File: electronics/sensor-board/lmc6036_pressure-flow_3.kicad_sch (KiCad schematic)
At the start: 12 parts, among them U14 LMC6036, U18 LMC6036

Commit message: work on sensor-board
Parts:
- removed U14, U18: LMC6036, LMC6036:SOP65P640X120-14N, symbol LMC6036_custom:LMC6036
- added U11: LMC6036, LMC6036:SOP65P640X120-14N, symbol LMC6036_custom:LMC6036
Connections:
- net VDD: now also U11.4 (VDD)
- net VSS: now also U11.11 (VSS)
- net output_A: now also U11.1 (OUTA), U11.2 (INA-)
- net output_B: now also U11.6 (INB-), U11.7 (OUTB)
- net output_C: now also U11.8 (OUTC), U11.9 (INC-)
- net output_D: now also U11.14 (OUTD)
- net at R103.1, R99.1: now also U11.5 (INB+)
- net at R101.1, R105.1: now also U11.12 (IND+)
- net at R106.1, R107.2: now also U11.13 (IND-)
- net at R100.1, R104.1: now also U11.10 (INC+)
- net at R102.1, R98.1: now also U11.3 (INA+)
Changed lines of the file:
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@@
   (junction (at 142.24 120.65) (diameter 0) (color 0 0 0 0))
   (junction (at 142.24 148.59) (diameter 0) (color 0 0 0 0))
-  (junction (at 147.32 143.51) (diameter 0) (color 0 0 0 0))
-  (junction (at 162.56 63.5) (diameter 0) (color 0 0 0 0))
-  (junction (at 162.56 90.17) (diameter 0) (color 0 0 0 0))
-  (junction (at 162.56 118.11) (diameter 0) (color 0 0 0 0))
-  (junction (at 162.56 146.05) (diameter 0) (color 0 0 0 0))
   (wire (pts (xy 125.73 60.96) (xy 135.89 60.96))
     (stroke (width 0) (type default) (color 0 0 0 0))
@@
   )
   (symbol (lib_id "Device:R") (at 135.89 148.59 270) (unit 1)
-    (in_bom yes) (on_board yes) (fields_autoplaced)
+    (in_bom yes) (on_board yes)
     (property "Reference" "R101" (id 0) (at 135.89 142.24 90))
-    (property "Value" "NO_RES" (id 1) (at 135.89 144.78 90))
+    (property "Value" "NO_RES" (id 1) (at 135.89 146.05 90))
     (property "Footprint" "Resistor_SMD:R_0603_1608Metric" (id 2) (at 135.89 146.812 90)
       (effects (font (size 1.27 1.27)) hide)
@@
   (symbol (lib_id "LMC6036_custom:LMC6036") (at 153.67 44.45 90) (unit 5)
     (in_bom yes) (on_board yes) (fields_autoplaced)
-    (property "Reference" "U14" (id 0) (at 153.67 35.56 90))
+    (property "Reference" "U11" (id 0) (at 153.67 35.56 90))
     (property "Value" "LMC6036" (id 1) (at 153.67 38.1 90))
     (property "Footprint" "LMC6036:SOP65P640X120-14N" (id 2) (at 153.67 42.545 0)
@@
   )
   (symbol (lib_id "LMC6036_custom:LMC6036") (at 153.67 63.5 0) (unit 1)
-    (in_bom yes) (on_board yes)
-    (property "Reference" "U18" (id 0) (at 154.94 53.34 0))
-    (property "Value" "LMC6036" (id 1) (at 160.02 68.58 0))
+    (in_bom yes) (on_board yes) (fields_autoplaced)
+    (property "Reference" "U11" (id 0) (at 154.94 53.34 0))
+    (property "Value" "LMC6036" (id 1) (at 154.94 55.88 0))
     (property "Footprint" "LMC6036:SOP65P640X120-14N" (id 2) (at 155.575 63.5 0)
       (effects (font (size 1.27 1.27)) hide)
@@
   (symbol (lib_id "LMC6036_custom:LMC6036") (at 153.67 90.17 0) (unit 2)
     (in_bom yes) (on_board yes) (fields_autoplaced)
-    (property "Reference" "U14" (id 0) (at 154.94 80.01 0))
+    (property "Reference" "U11" (id 0) (at 154.94 80.01 0))
     (property "Value" "LMC6036" (id 1) (at 154.94 82.55 0))
     (property "Footprint" "LMC6036:SOP65P640X120-14N" (id 2) (at 155.575 90.17 0)
@@
   (symbol (lib_id "LMC6036_custom:LMC6036") (at 153.67 118.11 0) (unit 3)
     (in_bom yes) (on_board yes) (fields_autoplaced)
-    (property "Reference" "U14" (id 0) (at 154.94 107.95 0))
+    (property "Reference" "U11" (id 0) (at 154.94 107.95 0))
     (property "Value" "LMC6036" (id 1) (at 154.94 110.49 0))
     (property "Footprint" "LMC6036:SOP65P640X120-14N" (id 2) (at 155.575 118.11 0)
@@
   (symbol (lib_id "LMC6036_custom:LMC6036") (at 153.67 146.05 0) (unit 4)
     (in_bom yes) (on_board yes)
-    (property "Reference" "U14" (id 0) (at 154.94 135.89 0))
-    (property "Value" "LMC6036" (id 1) (at 152.4 146.05 0))
+    (property "Reference" "U11" (id 0) (at 154.94 135.89 0))
+    (property "Value" "LMC6036" (id 1) (at 154.94 140.97 0))
     (property "Footprint" "LMC6036:SOP65P640X120-14N" (id 2) (at 155.575 146.05 0)
       (effects (font (size 1.27 1.27)) hide)

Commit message: work on sensor-board pcb
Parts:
- removed R101, R105, R106, R107: NO_RES, Resistor_SMD:R_0603_1608Metric, symbol Device:R
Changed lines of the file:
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@@
-    (pin "2")
-  )
-  (symbol (lib_id "Device:R") (at 135.89 143.51 270) (unit 1)
-    (in_bom yes) (on_board yes) (fields_autoplaced)
-    (property "Reference" "R106" (id 0) (at 135.89 137.16 90))
-    (property "Value" "NO_RES" (id 1) (at 135.89 139.7 90))
-    (property "Footprint" "Resistor_SMD:R_0603_1608Metric" (id 2) (at 135.89 141.732 90)
-      (effects (font (size 1.27 1.27)) hide)
-    )
-    (property "Datasheet" "~" (id 3) (at 135.89 143.51 0)
-      (effects (font (size 1.27 1.27)) hide)
-    )
-    (pin "1")
-    (pin "2")
-  )
-  (symbol (lib_id "Device:R") (at 135.89 148.59 270) (unit 1)
-    (in_bom yes) (on_board yes)
-    (property "Reference" "R101" (id 0) (at 135.89 142.24 90))
-    (property "Value" "NO_RES" (id 1) (at 135.89 146.05 90))
-    (property "Footprint" "Resistor_SMD:R_0603_1608Metric" (id 2) (at 135.89 146.812 90)
-      (effects (font (size 1.27 1.27)) hide)
-    )
-    (property "Datasheet" "~" (id 3) (at 135.89 148.59 0)
-      (effects (font (size 1.27 1.27)) hide)
-    )
-    (pin "1")
     (pin "2")
   )
@@
       (effects (font (size 1.27 1.27)) hide)
     )
-    (pin "1")
-    (pin "2")
-  )
-  (symbol (lib_id "Device:R") (at 142.24 153.67 0) (unit 1)
-    (in_bom yes) (on_board yes) (fields_autoplaced)
-    (property "Reference" "R105" (id 0) (at 144.78 152.3999 0)
-      (effects (font (size 1.27 1.27)) (justify left))
-    )
-    (property "Value" "NO_RES" (id 1) (at 144.78 154.9399 0)
-      (effects (font (size 1.27 1.27)) (justify left))
-    )
-    (property "Footprint" "Resistor_SMD:R_0603_1608Metric" (id 2) (at 140.462 153.67 90)
-      (effects (font (size 1.27 1.27)) hide)
-    )
-    (property "Datasheet" "~" (id 3) (at 142.24 153.67 0)
-      (effects (font (size 1.27 1.27)) hide)
-    )
-    (pin "1")
-    (pin "2")
-  )
-  (symbol (lib_id "Device:R") (at 154.94 138.43 270) (unit 1)
-    (in_bom yes) (on_board yes) (fields_autoplaced)
-    (property "Reference" "R107" (id 0) (at 154.94 132.08 90))
-    (property "Value" "NO_RES" (id 1) (at 154.94 134.62 90))
-    (property "Footprint" "Resistor_SMD:R_0603_1608Metric" (id 2) (at 154.94 136.652 90)
-      (effects (font (size 1.27 1.27)) hide)
-    )
-    (property "Datasheet" "~" (id 3) (at 154.94 138.43 0)
-      (effects (font (size 1.27 1.27)) hide)
-    )

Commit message: More work on sensor-board
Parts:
- R100, R103, R104, R98, R99: value 150 -> 100
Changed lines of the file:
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@@
       (effects (font (size 1.27 1.27)) (justify left))
     )
-    (property "Value" "150" (id 1) (at 144.78 99.0599 0)
+    (property "Value" "100" (id 1) (at 144.78 99.0599 0)
       (effects (font (size 1.27 1.27)) (justify left))
     )
@@
     (in_bom yes) (on_board yes) (fields_autoplaced)
     (property "Reference" "R99" (id 0) (at 135.89 86.36 90))
-    (property "Value" "150" (id 1) (at 135.89 88.9 90))
+    (property "Value" "100" (id 1) (at 135.89 88.9 90))
     (property "Footprint" "Resistor_SMD:R_0603_1608Metric" (id 2) (at 135.89 90.932 90)
       (effects (font (size 1.27 1.27)) hide)
@@
     (in_bom yes) (on_board yes) (fields_autoplaced)
     (property "Reference" "R100" (id 0) (at 135.89 114.3 90))
-    (property "Value" "150" (id 1) (at 135.89 116.84 90))
+    (property "Value" "100" (id 1) (at 135.89 116.84 90))
     (property "Footprint" "Resistor_SMD:R_0603_1608Metric" (id 2) (at 135.89 118.872 90)
       (effects (font (size 1.27 1.27)) hide)
@@
     (in_bom yes) (on_board yes) (fields_autoplaced)
     (property "Reference" "R98" (id 0) (at 135.89 59.69 90))
-    (property "Value" "150" (id 1) (at 135.89 62.23 90))
+    (property "Value" "100" (id 1) (at 135.89 62.23 90))
     (property "Footprint" "Resistor_SMD:R_0603_1608Metric" (id 2) (at 135.89 64.262 90)
       (effects (font (size 1.27 1.27)) hide)
@@
       (effects (font (size 1.27 1.27)) (justify left))
     )
-    (property "Value" "150" (id 1) (at 144.78 126.9999 0)
+    (property "Value" "100" (id 1) (at 144.78 126.9999 0)
       (effects (font (size 1.27 1.27)) (justify left))
     )

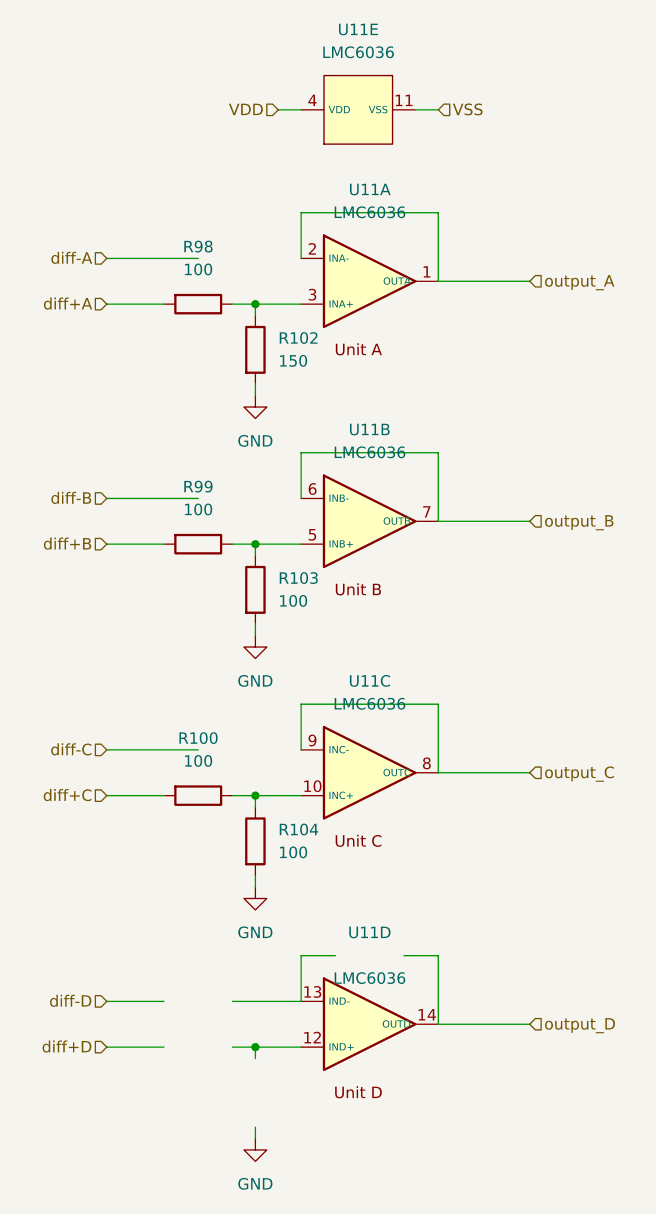
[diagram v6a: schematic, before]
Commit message: updated loadcell amplifier
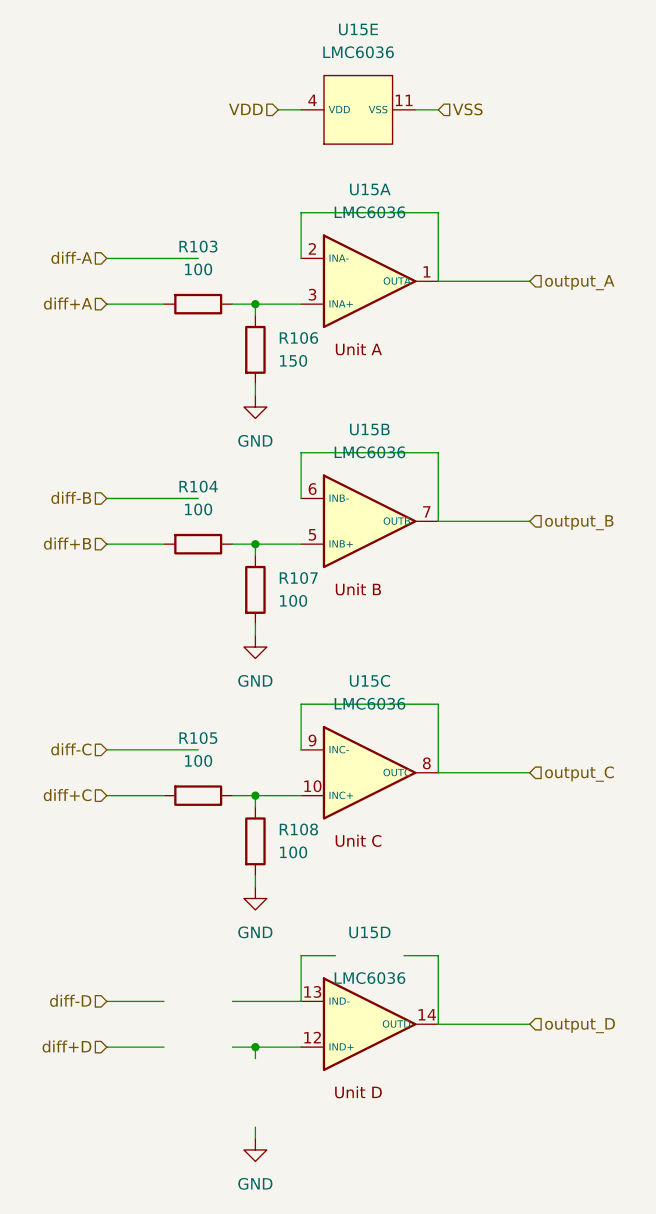
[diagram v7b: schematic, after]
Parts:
- renumbered R98 to R103, R99 to R104, R100 to R105, R102 to R106, R103 to R107, R104 to R108, U11 to U15
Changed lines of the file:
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@@
   (symbol (lib_id "power:GND") (at 142.24 158.75 0) (unit 1)
     (in_bom yes) (on_board yes) (fields_autoplaced)
-    (property "Reference" "#PWR0134" (id 0) (at 142.24 165.1 0)
+    (property "Reference" "#PWR0149" (id 0) (at 142.24 165.1 0)
       (effects (font (size 1.27 1.27)) hide)
     )
@@
   (symbol (lib_id "Device:R") (at 142.24 97.79 0) (unit 1)
     (in_bom yes) (on_board yes) (fields_autoplaced)
-    (property "Reference" "R103" (id 0) (at 144.78 96.5199 0)
+    (property "Reference" "R107" (id 0) (at 144.78 96.5199 0)
       (effects (font (size 1.27 1.27)) (justify left))
     )
@@
   (symbol (lib_id "power:GND") (at 142.24 76.2 0) (unit 1)
     (in_bom yes) (on_board yes) (fields_autoplaced)
-    (property "Reference" "#PWR0131" (id 0) (at 142.24 82.55 0)
+    (property "Reference" "#PWR0146" (id 0) (at 142.24 82.55 0)
       (effects (font (size 1.27 1.27)) hide)
     )
@@
   (symbol (lib_id "Device:R") (at 135.89 92.71 270) (unit 1)
     (in_bom yes) (on_board yes) (fields_autoplaced)
-    (property "Reference" "R99" (id 0) (at 135.89 86.36 90))
+    (property "Reference" "R104" (id 0) (at 135.89 86.36 90))
     (property "Value" "100" (id 1) (at 135.89 88.9 90))
     (property "Footprint" "Resistor_SMD:R_0603_1608Metric" (id 2) (at 135.89 90.932 90)
@@
   (symbol (lib_id "LMC6036_custom:LMC6036") (at 153.67 146.05 0) (unit 4)
     (in_bom yes) (on_board yes)
-    (property "Reference" "U11" (id 0) (at 154.94 135.89 0))
+    (property "Reference" "U15" (id 0) (at 154.94 135.89 0))
     (property "Value" "LMC6036" (id 1) (at 154.94 140.97 0))
     (property "Footprint" "LMC6036:SOP65P640X120-14N" (id 2) (at 155.575 146.05 0)
@@
   (symbol (lib_id "Device:R") (at 135.89 120.65 270) (unit 1)
     (in_bom yes) (on_board yes) (fields_autoplaced)
-    (property "Reference" "R100" (id 0) (at 135.89 114.3 90))
+    (property "Reference" "R105" (id 0) (at 135.89 114.3 90))
     (property "Value" "100" (id 1) (at 135.89 116.84 90))
     (property "Footprint" "Resistor_SMD:R_0603_1608Metric" (id 2) (at 135.89 118.872 90)
@@
   (symbol (lib_id "LMC6036_custom:LMC6036") (at 153.67 63.5 0) (unit 1)
     (in_bom yes) (on_board yes) (fields_autoplaced)
-    (property "Reference" "U11" (id 0) (at 154.94 53.34 0))
+    (property "Reference" "U15" (id 0) (at 154.94 53.34 0))
     (property "Value" "LMC6036" (id 1) (at 154.94 55.88 0))
     (property "Footprint" "LMC6036:SOP65P640X120-14N" (id 2) (at 155.575 63.5 0)
@@
   (symbol (lib_id "power:GND") (at 142.24 130.81 0) (unit 1)
     (in_bom yes) (on_board yes) (fields_autoplaced)
-    (property "Reference" "#PWR0133" (id 0) (at 142.24 137.16 0)
+    (property "Reference" "#PWR0148" (id 0) (at 142.24 137.16 0)
       (effects (font (size 1.27 1.27)) hide)
     )
@@
   (symbol (lib_id "Device:R") (at 135.89 66.04 270) (unit 1)
     (in_bom yes) (on_board yes) (fields_autoplaced)
-    (property "Reference" "R98" (id 0) (at 135.89 59.69 90))
+    (property "Reference" "R103" (id 0) (at 135.89 59.69 90))
     (property "Value" "100" (id 1) (at 135.89 62.23 90))
     (property "Footprint" "Resistor_SMD:R_0603_1608Metric" (id 2) (at 135.89 64.262 90)
@@
   (symbol (lib_id "power:GND") (at 142.24 102.87 0) (unit 1)
     (in_bom yes) (on_board yes) (fields_autoplaced)
-    (property "Reference" "#PWR0132" (id 0) (at 142.24 109.22 0)
+    (property "Reference" "#PWR0147" (id 0) (at 142.24 109.22 0)
       (effects (font (size 1.27 1.27)) hide)
     )
@@
   (symbol (lib_id "LMC6036_custom:LMC6036") (at 153.67 90.17 0) (unit 2)
     (in_bom yes) (on_board yes) (fields_autoplaced)
-    (property "Reference" "U11" (id 0) (at 154.94 80.01 0))
+    (property "Reference" "U15" (id 0) (at 154.94 80.01 0))
     (property "Value" "LMC6036" (id 1) (at 154.94 82.55 0))
     (property "Footprint" "LMC6036:SOP65P640X120-14N" (id 2) (at 155.575 90.17 0)
@@
   (symbol (lib_id "LMC6036_custom:LMC6036") (at 153.67 44.45 90) (unit 5)
     (in_bom yes) (on_board yes) (fields_autoplaced)
-    (property "Reference" "U11" (id 0) (at 153.67 35.56 90))
+    (property "Reference" "U15" (id 0) (at 153.67 35.56 90))
     (property "Value" "LMC6036" (id 1) (at 153.67 38.1 90))
     (property "Footprint" "LMC6036:SOP65P640X120-14N" (id 2) (at 153.67 42.545 0)
@@
   (symbol (lib_id "Device:R") (at 142.24 125.73 0) (unit 1)
     (in_bom yes) (on_board yes) (fields_autoplaced)
-    (property "Reference" "R104" (id 0) (at 144.78 124.4599 0)
+    (property "Reference" "R108" (id 0) (at 144.78 124.4599 0)
       (effects (font (size 1.27 1.27)) (justify left))
     )
@@
   (symbol (lib_id "LMC6036_custom:LMC6036") (at 153.67 118.11 0) (unit 3)
     (in_bom yes) (on_board yes) (fields_autoplaced)
-    (property "Reference" "U11" (id 0) (at 154.94 107.95 0))
+    (property "Reference" "U15" (id 0) (at 154.94 107.95 0))
     (property "Value" "LMC6036" (id 1) (at 154.94 110.49 0))
     (property "Footprint" "LMC6036:SOP65P640X120-14N" (id 2) (at 155.575 118.11 0)
@@
   (symbol (lib_id "Device:R") (at 142.24 71.12 0) (unit 1)
     (in_bom yes) (on_board yes) (fields_autoplaced)
-    (property "Reference" "R102" (id 0) (at 144.78 69.8499 0)
-      (effects (font (size 1.27 1.27)) (justify left))
-    )
+    (property "Reference" "R106" (id 0) (at 144.78 69.8499 0)
+      (effects (font (size 1.27 1.27)) (justify left))
+    )

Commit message: res value fix
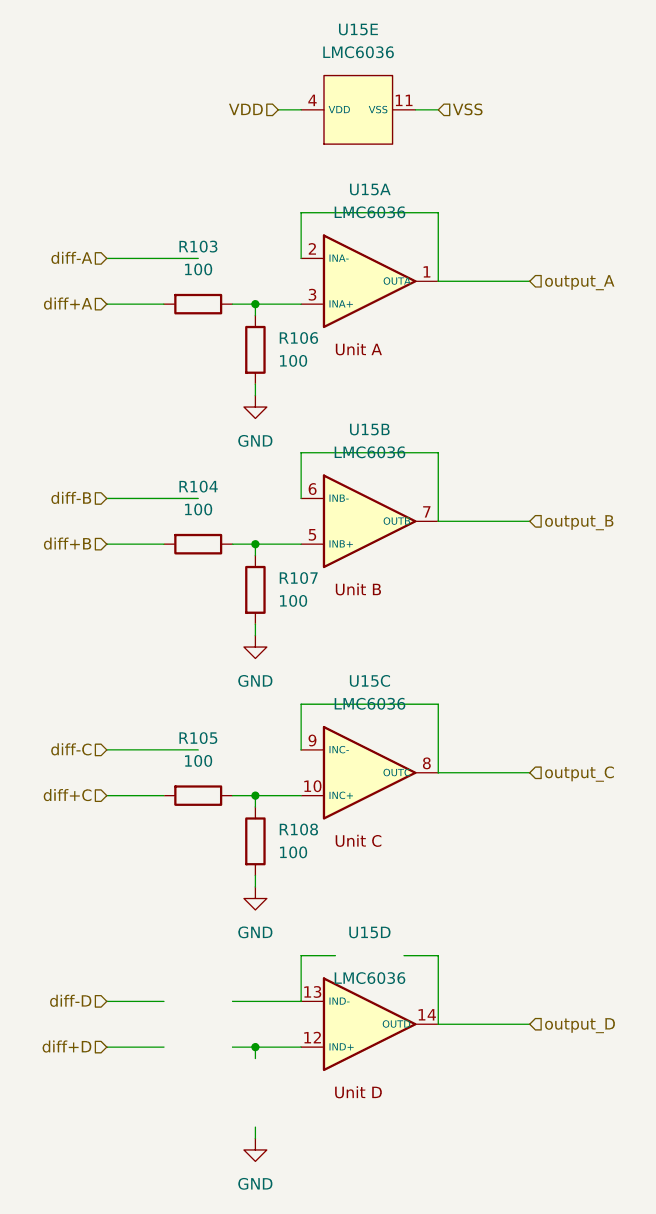
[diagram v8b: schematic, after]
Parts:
- R106: value 150 -> 100
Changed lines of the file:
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@@
       (effects (font (size 1.27 1.27)) (justify left))
     )
-    (property "Value" "150" (id 1) (at 144.78 72.3899 0)
+    (property "Value" "100" (id 1) (at 144.78 72.3899 0)
       (effects (font (size 1.27 1.27)) (justify left))
     )
